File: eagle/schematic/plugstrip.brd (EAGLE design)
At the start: 109.2 x 86.4 mm, 30 parts, among them U1 Hall Effect, U2 Current ADC, U3 Voltage ADC

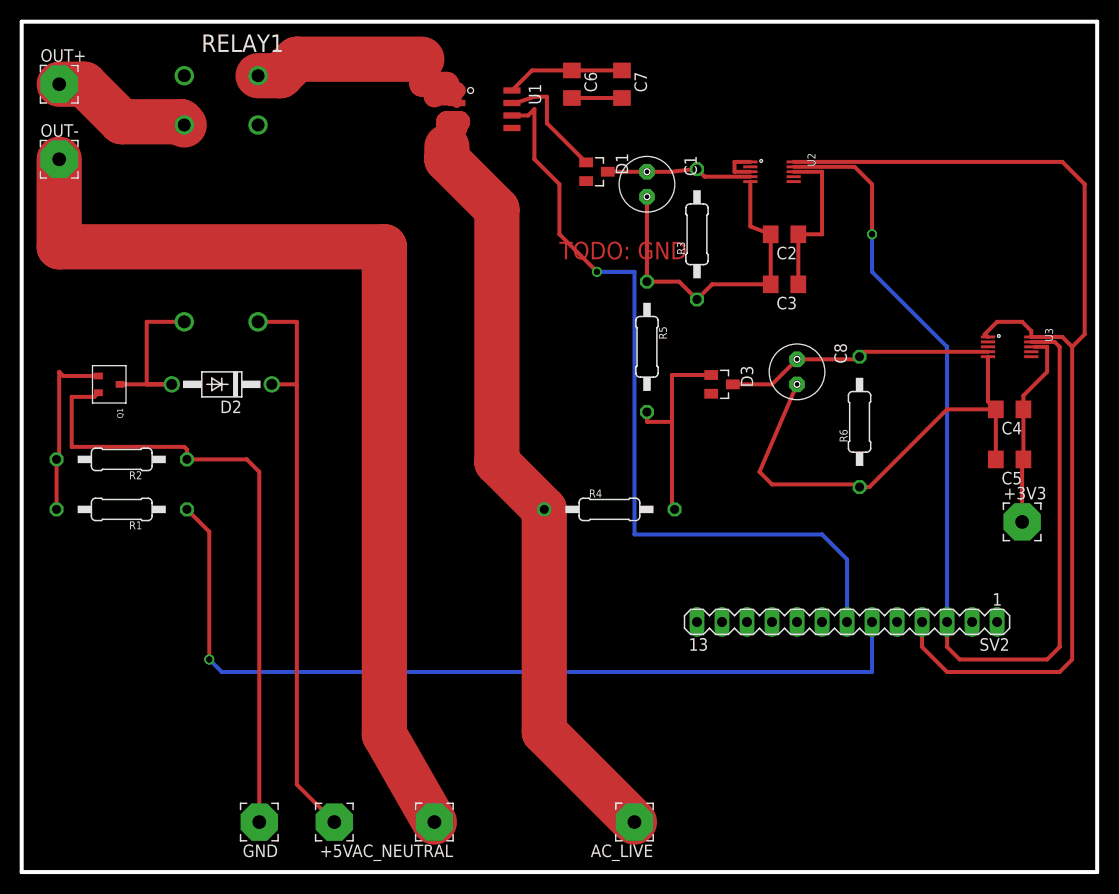
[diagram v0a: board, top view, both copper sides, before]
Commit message: add fuse, remove ground routing
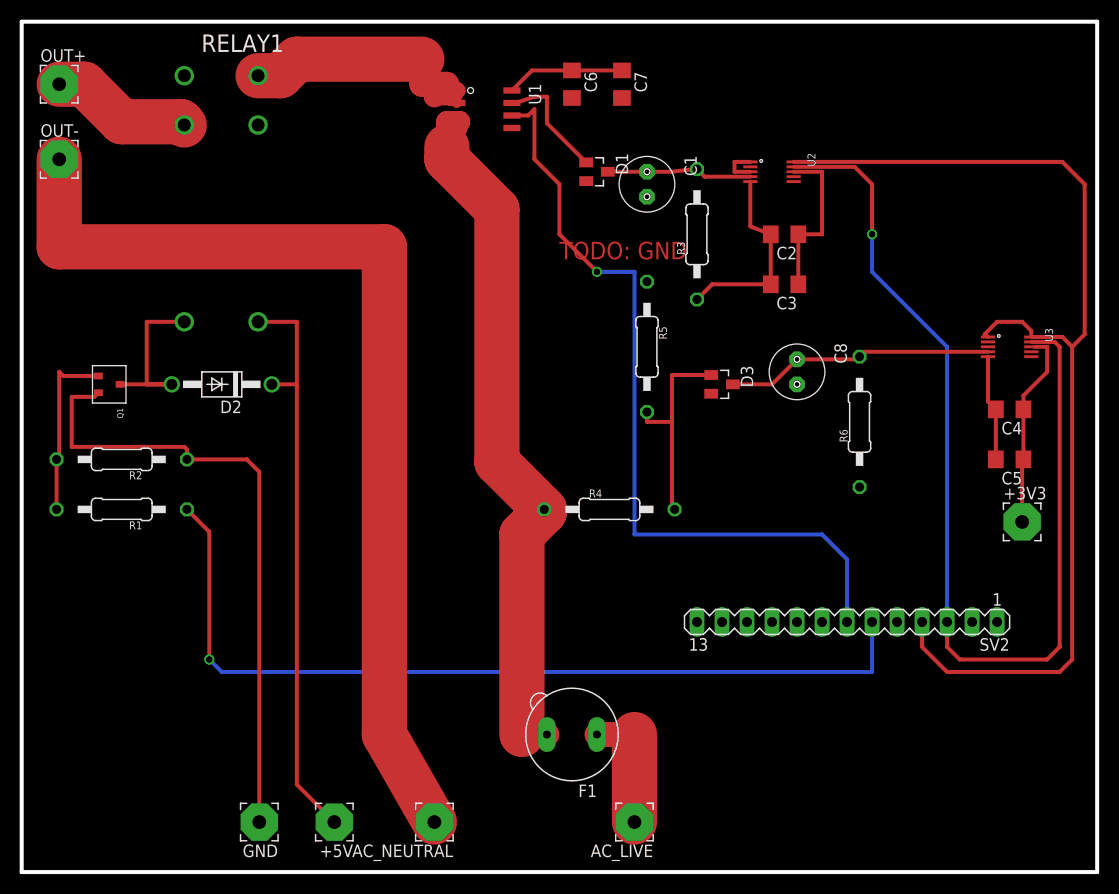
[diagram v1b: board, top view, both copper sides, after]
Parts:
- added F1: (no value), fuse:19560
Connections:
- new net N$14: AC_LIVE.1, F1.1
- net AC_LIVE: now also F1.2; no longer AC_LIVE.1
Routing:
- net GND: track 156.3 -> 99.2 mm
- net N$14: track 0.00 -> 12.7 mm
- net AC_LIVE: track 81.0 -> 71.8 mm
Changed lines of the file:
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@@
 <element name="C8" library="jackIdd" package="C2.5-2" value="1uF" x="77.47" y="49.53" rot="R270"/>
 <element name="R6" library="jackIdd" package="0411/15" value="200K" x="83.82" y="44.45" rot="R90"/>
+<element name="F1" library="fuse" package="19560" value="" x="54.61" y="12.7" rot="R180">
+<attribute name="OC_FARNELL" value="1185363" x="54.61" y="12.7" size="1.778" layer="27" rot="R180" display="off"/>
+<attribute name="MPN" value="56000001009" x="54.61" y="12.7" size="1.778" layer="27" rot="R180" display="off"/>
+<attribute name="OC_NEWARK" value="15P8392" x="54.61" y="12.7" size="1.778" layer="27" rot="R180" display="off"/>
+<attribute name="MF" value="" x="54.61" y="12.7" size="1.778" layer="27" rot="R180" display="off"/>
+</element>
 </elements>
 <signals>
@@
 <wire x1="21.59" y1="40.64" x2="22.86" y2="39.37" width="0.4064" layer="1"/>
 <wire x1="22.86" y1="39.37" x2="22.86" y2="3.81" width="0.4064" layer="1"/>
-<wire x1="77.47" y1="48.26" x2="73.66" y2="39.37" width="0.4064" layer="1"/>
-<wire x1="73.66" y1="39.37" x2="74.93" y2="38.1" width="0.4064" layer="1"/>
-<wire x1="74.93" y1="38.1" x2="83.55" y2="38.1" width="0.4064" layer="1"/>
-<wire x1="83.55" y1="38.1" x2="83.82" y2="37.83" width="0.4064" layer="1"/>
 <wire x1="74.8" y1="58.42" x2="74.8" y2="63.5" width="0.4064" layer="1"/>
-<wire x1="54.61" y1="77.34" x2="59.69" y2="77.34" width="0.4064" layer="1"/>
 <wire x1="72.73" y1="68.85" x2="72.73" y2="64.3" width="0.4064" layer="1"/>
 <wire x1="72.73" y1="64.3" x2="74.8" y2="63.5" width="0.4064" layer="1"/>
@@
 <wire x1="71.12" y1="69.85" x2="72.73" y2="69.85" width="0.4064" layer="1"/>
 <wire x1="97.66" y1="40.64" x2="97.66" y2="45.72" width="0.4064" layer="1"/>
-<wire x1="83.82" y1="37.83" x2="84.82" y2="37.83" width="0.4064" layer="1"/>
-<wire x1="84.82" y1="37.83" x2="92.71" y2="45.72" width="0.4064" layer="1"/>
-<wire x1="92.71" y1="45.72" x2="97.66" y2="45.72" width="0.4064" layer="1"/>
 <wire x1="96.86" y1="51.07" x2="96.86" y2="46.52" width="0.4064" layer="1"/>
 <wire x1="96.86" y1="46.52" x2="97.66" y2="45.72" width="0.4064" layer="1"/>
-<wire x1="67.31" y1="56.88" x2="65.5" y2="58.69" width="0.4064" layer="1"/>
-<wire x1="65.5" y1="58.69" x2="62.23" y2="58.69" width="0.4064" layer="1"/>
-<wire x1="62.23" y1="67.31" x2="62.23" y2="58.69" width="0.4064" layer="1"/>
+<wire x1="67.31" y1="56.88" x2="68.85" y2="58.42" width="0.4064" layer="1"/>
+<wire x1="68.85" y1="58.42" x2="74.8" y2="58.42" width="0.4064" layer="1"/>
 <wire x1="96.86" y1="51.07" x2="96.86" y2="52.07" width="0" layer="19" extent="1-1"/>
+<wire x1="83.82" y1="37.83" x2="97.66" y2="40.64" width="0" layer="19" extent="1-1"/>
+<wire x1="77.47" y1="48.26" x2="83.82" y2="37.83" width="0" layer="19" extent="1-1"/>
 <wire x1="74.8" y1="58.42" x2="77.47" y2="48.26" width="0" layer="19" extent="1-1"/>
 <wire x1="72.73" y1="69.85" x2="72.73" y2="68.85" width="0" layer="19" extent="1-1"/>
+<wire x1="62.23" y1="58.69" x2="67.31" y2="56.88" width="0" layer="19" extent="1-1"/>
+<wire x1="62.23" y1="67.31" x2="62.23" y2="58.69" width="0" layer="19" extent="1-1"/>
 <wire x1="59.69" y1="77.34" x2="62.23" y2="67.31" width="0" layer="19" extent="1-1"/>
+<wire x1="54.61" y1="77.34" x2="59.69" y2="77.34" width="0" layer="19" extent="1-1"/>
 <wire x1="48.52" y1="74.295" x2="54.61" y2="77.34" width="0" layer="19" extent="1-1"/>
 <wire x1="21.59" y1="40.64" x2="48.52" y2="74.295" width="0" layer="19" extent="1-1"/>
-<wire x1="67.31" y1="56.88" x2="68.85" y2="58.42" width="0.4064" layer="1"/>
-<wire x1="68.85" y1="58.42" x2="74.8" y2="58.42" width="0.4064" layer="1"/>
 </signal>
 <signal name="+3V3">
@@
 <contactref element="U1" pad="P$4"/>
 <contactref element="R4" pad="1"/>
-<contactref element="AC_LIVE" pad="1"/>
-<wire x1="60.96" y1="3.81" x2="51.8" y2="12.97" width="4.5974" layer="1"/>
-<wire x1="51.8" y1="12.97" x2="51.8" y2="35.56" width="4.5974" layer="1"/>
 <wire x1="51.8" y1="35.56" x2="46.99" y2="40.37" width="4.5974" layer="1"/>
 <wire x1="46.99" y1="40.37" x2="46.99" y2="66.04" width="4.5974" layer="1"/>
@@
 <wire x1="43.18" y1="74.93" x2="42.92" y2="74.67" width="2.1844" layer="1"/>
 <wire x1="42.92" y1="74.67" x2="42.92" y2="74.295" width="2.1844" layer="1"/>
+<contactref element="F1" pad="2"/>
 <wire x1="43.18" y1="74.93" x2="42.92" y2="75.565" width="0" layer="19" extent="1-1"/>
+<wire x1="49.53" y1="12.7" x2="49.53" y2="33.02" width="4.5974" layer="1"/>
+<wire x1="49.53" y1="33.02" x2="51.8" y2="35.29" width="4.5974" layer="1"/>
+<wire x1="51.8" y1="35.29" x2="51.8" y2="35.56" width="4.5974" layer="1"/>
+<wire x1="52.07" y1="12.7" x2="49.53" y2="12.7" width="2.54" layer="1"/>
 </signal>
 <signal name="N$31">
@@
 <via x="57.15" y="59.69" extent="1-16" drill="0.6096" shape="square"/>
 </signal>
+<signal name="N$14" class="1">
+<contactref element="AC_LIVE" pad="1"/>
+<contactref element="F1" pad="1"/>
+<wire x1="60.96" y1="3.81" x2="60.96" y2="12.7" width="4.5974" layer="1"/>
+<wire x1="60.96" y1="12.7" x2="57.15" y2="12.7" width="2.54" layer="1"/>
+</signal>
 </signals>
